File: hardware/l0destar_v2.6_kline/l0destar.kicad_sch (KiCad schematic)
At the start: 10 parts

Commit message: tweaked layouts
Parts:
- removed S1NT1: NetTie_2, symbol Device:NetTie_2
- removed S1R3: 100K, Resistor_SMD:R_0402_1005Metric, symbol Device:R
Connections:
- net VSYS: no longer names the net of S1J2.2 (VSYS)

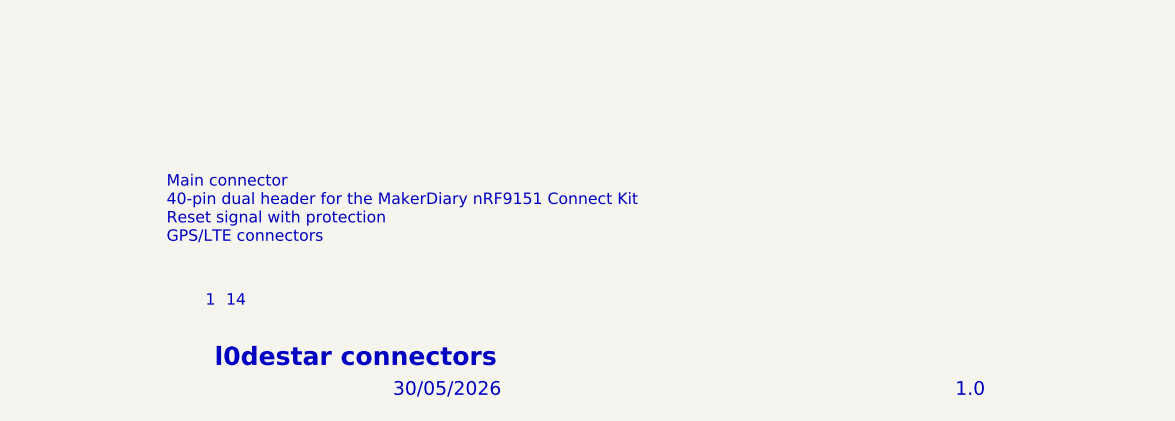
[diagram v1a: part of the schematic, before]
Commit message: fix sheet annotations
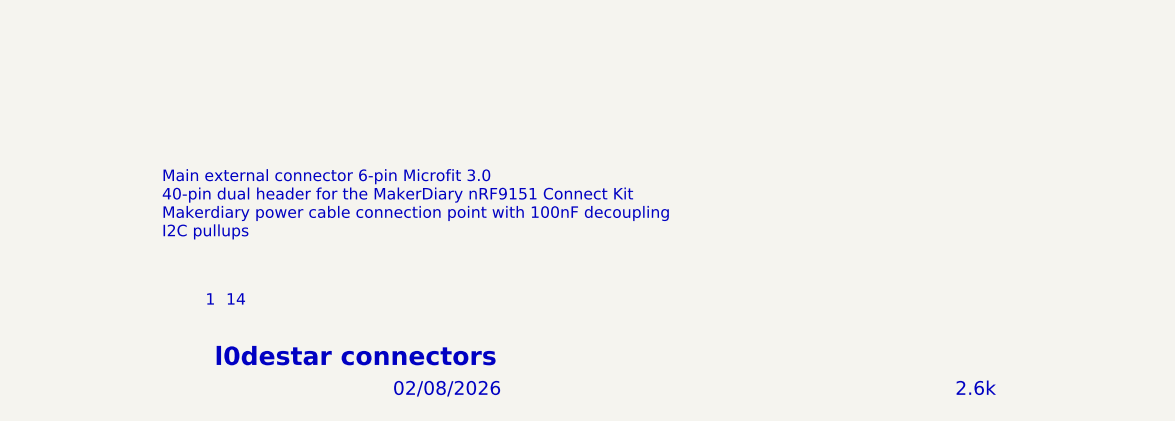
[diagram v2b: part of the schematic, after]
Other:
- note added: "02/08/2026"
- note added: "2.6k"
- note added: "Main external connector 6-pin Microfit 3.0 40-pin dual header for the MakerDiary nRF9151 Connect Kit Makerdiary power cable connection point with 100nF decoupling I2C pullups"
- note removed: "1.0"
- note removed: "30/05/2026"
- note removed: "Main connector 40-pin dual header for the MakerDiary nRF9151 Connect Kit Reset signal with protection GPS/LTE connectors"
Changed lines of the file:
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@@
 		)
 	)
-	(text "Main connector\n40-pin dual header for the MakerDiary nRF9151 Connect Kit\nReset signal with protection\nGPS/LTE connectors"
+	(text "Main external connector 6-pin Microfit 3.0\n40-pin dual header for the MakerDiary nRF9151 Connect Kit\nMakerdiary power cable connection point with 100nF decoupling\nI2C pullups"
 		(exclude_from_sim no)
-		(at 180.848 173.228 0)
+		(at 180.34 172.72 0)
 		(effects
 			(font
@@
 		)
 	)
-	(text "30/05/2026"
+	(text "02/08/2026"
 		(exclude_from_sim no)
 		(at 205.994 193.294 0)
@@
 		)
 	)
-	(text "1.0"
+	(text "2.6k"
 		(exclude_from_sim no)
 		(at 268.478 193.294 0)
